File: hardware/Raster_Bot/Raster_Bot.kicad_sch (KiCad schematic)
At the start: 68 parts, among them J1 JST_PH, J2 USB_C_Receptacle_USB2.0_16P, J3 Conn_Motor_N20_Encoder, J4 Conn_EYESPI, J5 JUMPER_2PIN, J6 Conn_Motor_N20_Encoder, J8 JUMPER_2PIN, Q1 AO3401A, SW1 SW_SPDT_SH, SW2 SW_RESET, SW3 SW_BOOT, U1 BQ24072RGT, U2 ESP32-S3-WROOM-1, U3 DRV8833PWPR, U4 AP2114H-3.3, U5 TPS61023DRLR

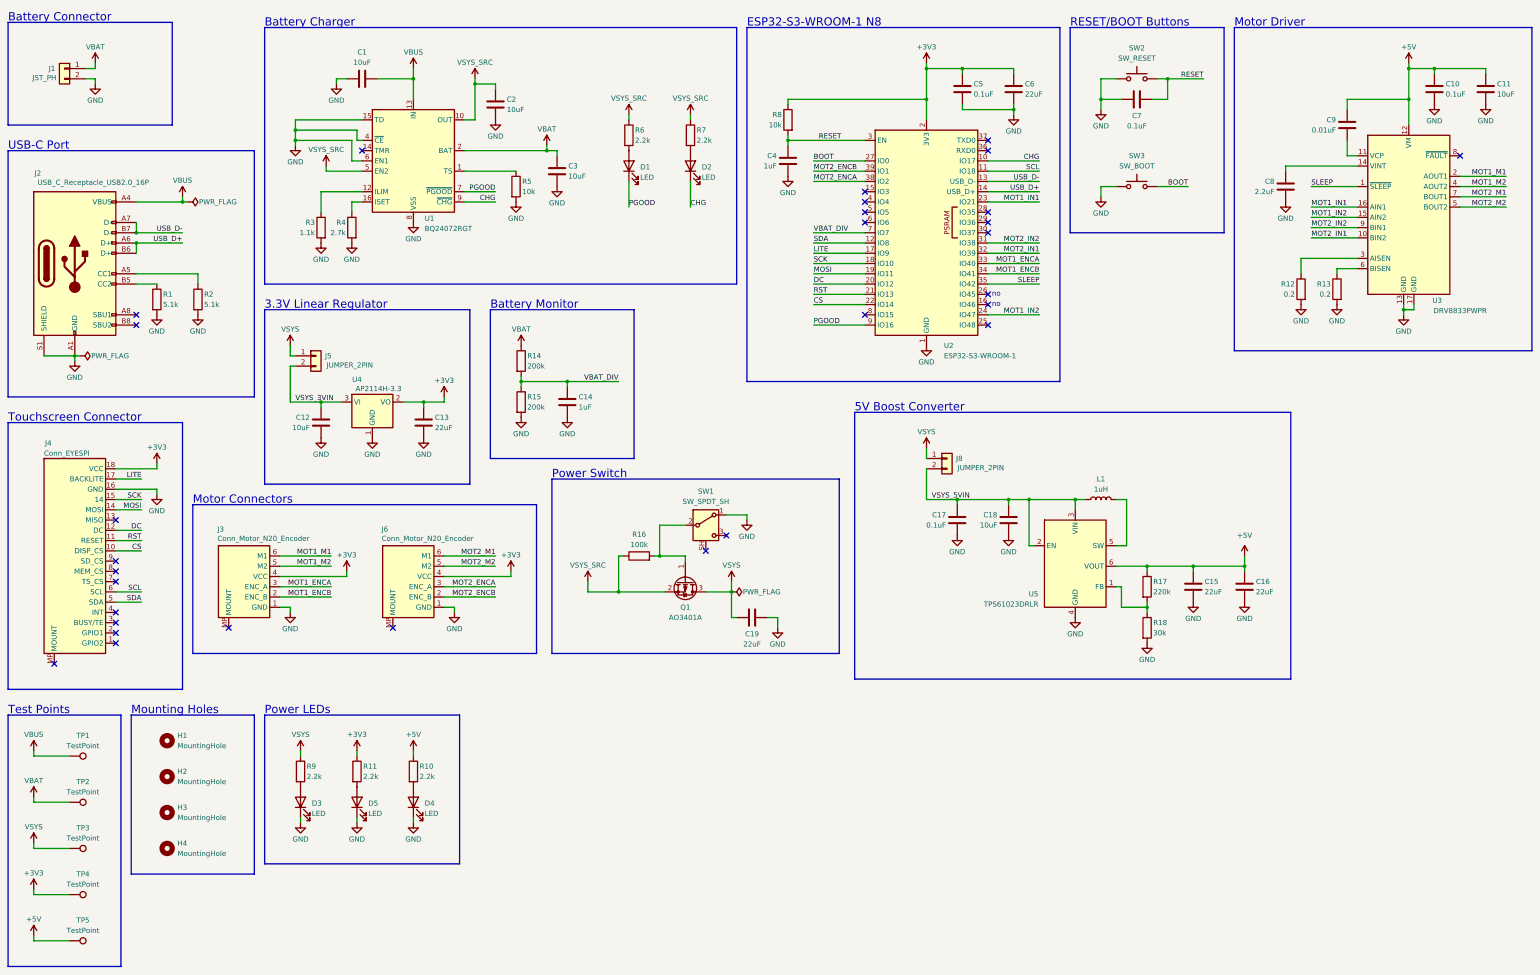
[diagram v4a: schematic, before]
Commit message: [hardware] v0.4 - 4 layer PCB design with ESP32-S3-MINI
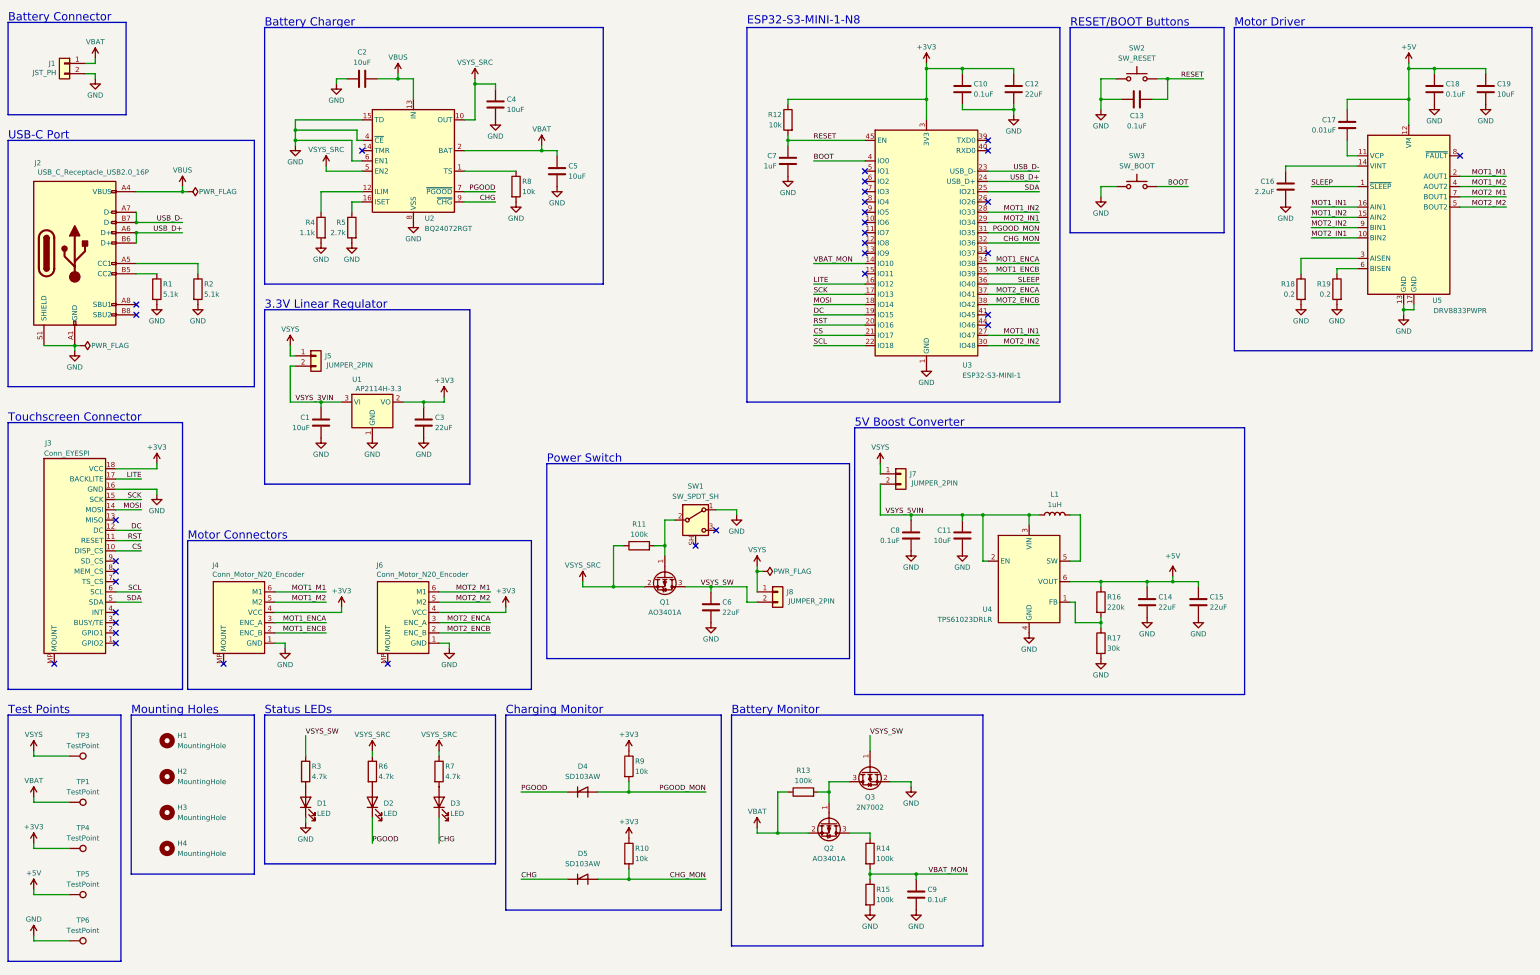
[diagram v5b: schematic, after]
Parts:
- removed C14, C4: 1uF, Capacitor_SMD:C_0603_1608Metric, symbol Device:C
- removed C19: 22uF, Capacitor_SMD:C_0805_2012Metric, symbol Device:C
- removed C5: 0.1uF, Capacitor_SMD:C_0603_1608Metric, symbol Device:C
- removed D4, D5: LED, LED_SMD:LED_0805_2012Metric, symbol Device:LED
- removed R16: 100k, Resistor_SMD:R_0603_1608Metric, symbol Device:R
- removed R8: 10k, Resistor_SMD:R_0603_1608Metric, symbol Device:R
- removed TP2: TestPoint, TestPoint:TestPoint_Pad_1.5x1.5mm, symbol Connector:TestPoint
- removed U2: ESP32-S3-WROOM-1, Raster_Bot:ESP32-S3-WROOM-1, symbol RF_Module:ESP32-S3-WROOM-1
- added C10, C9: 0.1uF, Capacitor_SMD:C_0603_1608Metric, symbol Device:C
- added C12: 22uF, Capacitor_SMD:C_0805_2012Metric, symbol Device:C
- added C7: 1uF, Capacitor_SMD:C_0603_1608Metric, symbol Device:C
- added D4, D5: SD103AW, Diode_SMD:D_SOD-123, symbol Device:D_Shockley
- added J8: JUMPER_2PIN, Connector_PinHeader_2.54mm:PinHeader_1x02_P2.54mm_Vertical, symbol Connector_Generic:Conn_01x02
- added Q2: AO3401A, Package_TO_SOT_SMD:SOT-23, symbol Transistor_FET:AO3401A
- added Q3: 2N7002, Package_TO_SOT_SMD:SOT-23, symbol Transistor_FET:2N7002
- added R12, R9: 10k, Resistor_SMD:R_0603_1608Metric, symbol Device:R
- added R13: 100k, Resistor_SMD:R_0603_1608Metric, symbol Device:R
- added TP6: TestPoint, TestPoint:TestPoint_Pad_1.5x1.5mm, symbol Connector:TestPoint
- added U3: ESP32-S3-MINI-1, Raster_Bot:ESP32-S3-MINI-1, symbol RF_Module:ESP32-S3-MINI-1
- H1, H2, H3, H4: footprint MountingHole:MountingHole_3.2mm_M3 -> MountingHole:MountingHole_2.7mm_M2.5
- R10: value 2.2k -> 10k; LCSC C4190 -> C25804
- R11: value 2.2k -> 100k; LCSC C4190 -> C25803
- R14, R15: value 200k -> 100k; LCSC C25811 -> C25803
- R3: renamed from R9; value 2.2k -> 4.7k; LCSC C4190 -> C23162
- R6, R7: value 2.2k -> 4.7k; LCSC C4190 -> C23162
- renumbered C12 to C1, C18 to C11, C7 to C13, C15 to C14, C16 to C15, C8 to C16, C9 to C17, C10 to C18, C11 to C19, C1 to C2, C13 to C3, C2 to C4, C3 to C5, C17 to C8, D3 to D1, D1 to D2, D2 to D3, J4 to J3, J3 to J4, J8 to J7, R17 to R16, R18 to R17, R12 to R18, R13 to R19, R3 to R4, R4 to R5, R5 to R8, U4 to U1, U1 to U2, U5 to U4, U3 to U5
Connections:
- net +3V3: now also R10.1, C10.1, C12.1, R12.1, R9.1, U3.3 (3V3); no longer C6.1, R11.1
- net +5V: no longer R10.1
- net BOOT: now also U3.4 (IO0)
- net CHG: now also D5.1 (K)
- net CS: now also U3.21 (IO17)
- net DC: now also U3.19 (IO15)
- net GND: now also C10.2, C12.2, C7.2, C9.2, Q3.2 (S), TP6.1, U3.1 (GND), U3.2 (GND), U3.42 (GND), U3.43 (GND), U3.46 (GND), U3.47 (GND), U3.48 (GND), U3.49 (GND), U3.50 (GND), U3.51 (GND), U3.52 (GND), U3.53 (GND), U3.54 (GND), U3.55 (GND), U3.56 (GND), U3.57 (GND), U3.58 (GND), U3.59 (GND), U3.60 (GND), U3.61 (GND), U3.62 (GND), U3.63 (GND), U3.64 (GND), U3.65 (GND)
- net LITE: now also U3.16 (IO12)
- net MOSI: now also U3.18 (IO14)
- net MOT1_ENCA: now also U3.34 (IO38)
- net MOT1_ENCB: now also U3.35 (IO39)
- net MOT1_IN1: now also U3.27 (IO47)
- net MOT1_IN2: now also U3.28 (IO33)
- net MOT2_ENCA: now also U3.37 (IO41)
- net MOT2_ENCB: now also U3.38 (IO42)
- net MOT2_IN1: now also U3.29 (IO34)
- net MOT2_IN2: now also U3.30 (IO48)
- net PGOOD: now also D4.1 (K)
- net RESET: now also C7.1, R12.2, U3.45 (EN)
- net RST: now also U3.20 (IO16)
- net SCK: now also U3.17 (IO13)
- net SCL: now also U3.22 (IO18)
- net SDA: now also U3.25 (IO21)
- net SLEEP: now also U3.36 (IO40)
- net USB_D+: now also U3.24 (USB_D+)
- net USB_D-: now also U3.23 (USB_D-)
- net VBAT: now also TP1.1, Q2.2 (S), R13.1; no longer R14.1
- net VBUS: no longer TP1.1
- net VSYS: now also J8.1 (Pin_1); no longer Q1.3 (D), R3.1
- net VSYS_SRC: now also R11.1
- net at R11.2: now also Q1.1 (G), SW1.2 (B)
- net CHG_MON: now reaches R10.2
- net CHG_MON: now also D5.2 (A), U3.32 (IO36)
- net VBAT_DIV renamed VBAT_MON
- net VBAT_MON: now also C9.1, U3.14 (IO10)
- new net: Q2.3 (D), R14.1
- new net: Q2.1 (G), Q3.3 (D), R13.2
- new net PGOOD_MON: D4.2 (A), R9.2, U3.31 (IO35)
- new net VSYS_SW: C6.1, J8.2 (Pin_2), Q1.3 (D), Q3.1 (G), R3.1
- no-connect marks 30 -> 33
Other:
- note added: "Charging Monitor"
- note added: "ESP32-S3-MINI-1-N8"
- note added: "Status LEDs"
- note removed: "ESP32-S3-WROOM-1 N8"
- note removed: "Power LEDs"
- note removed: "no"
- moved on the sheet: C11, C14, C15, C8, D1, D2, D3, J1, J2, J4, J6, J7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

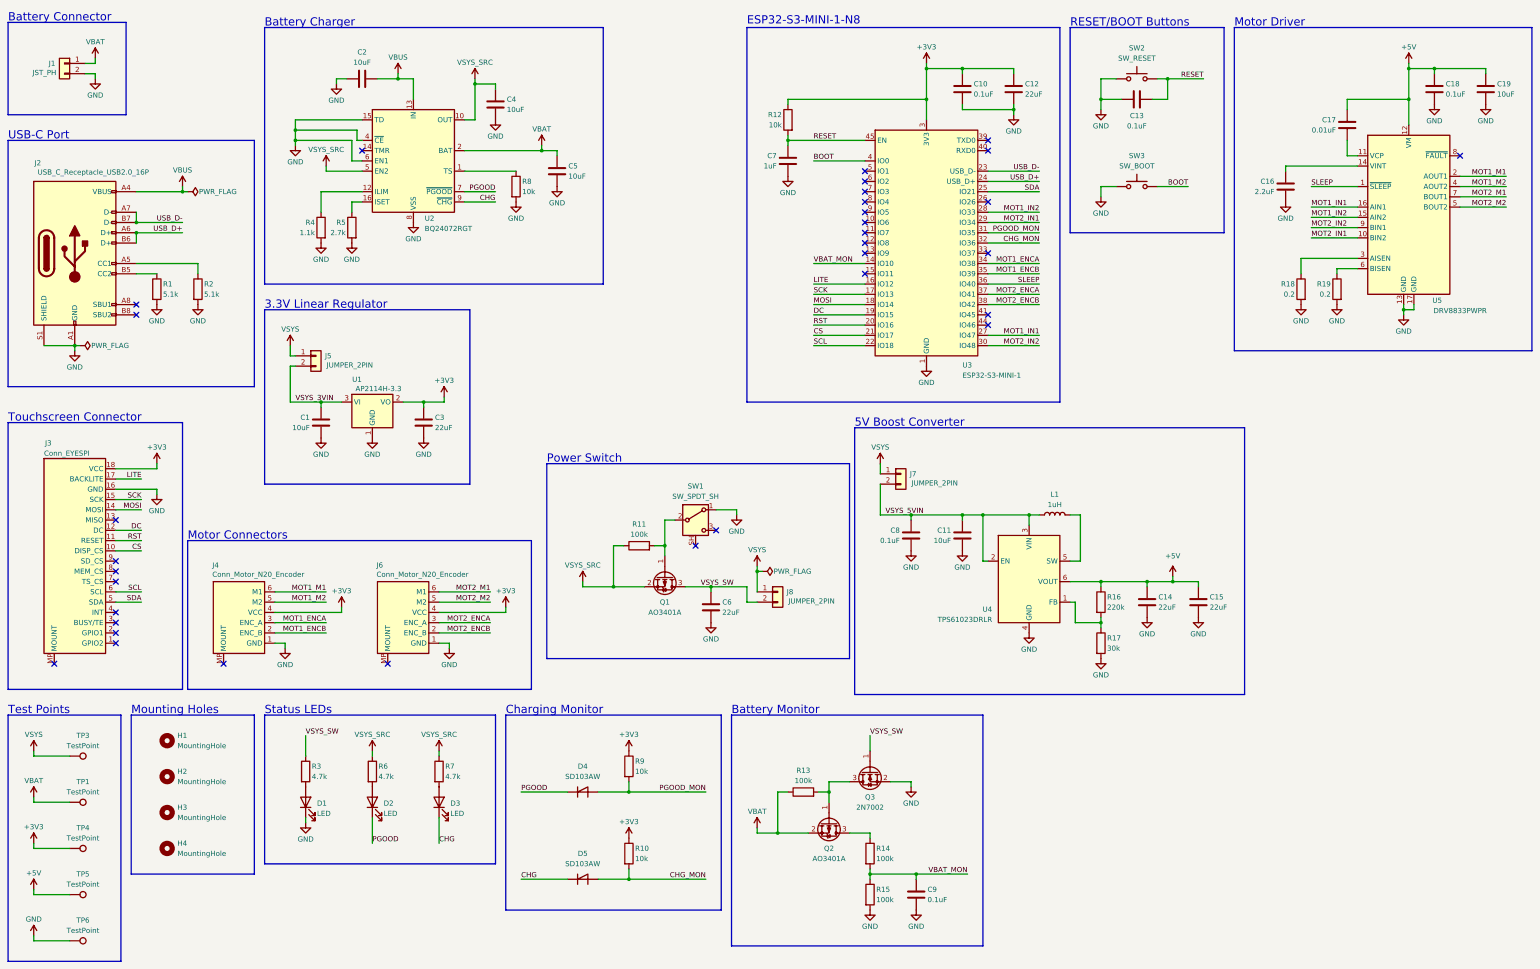
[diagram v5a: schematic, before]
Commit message: [hardware] v0.5 - Add motor driver bulk capacitor; Remove test pads and jumpers
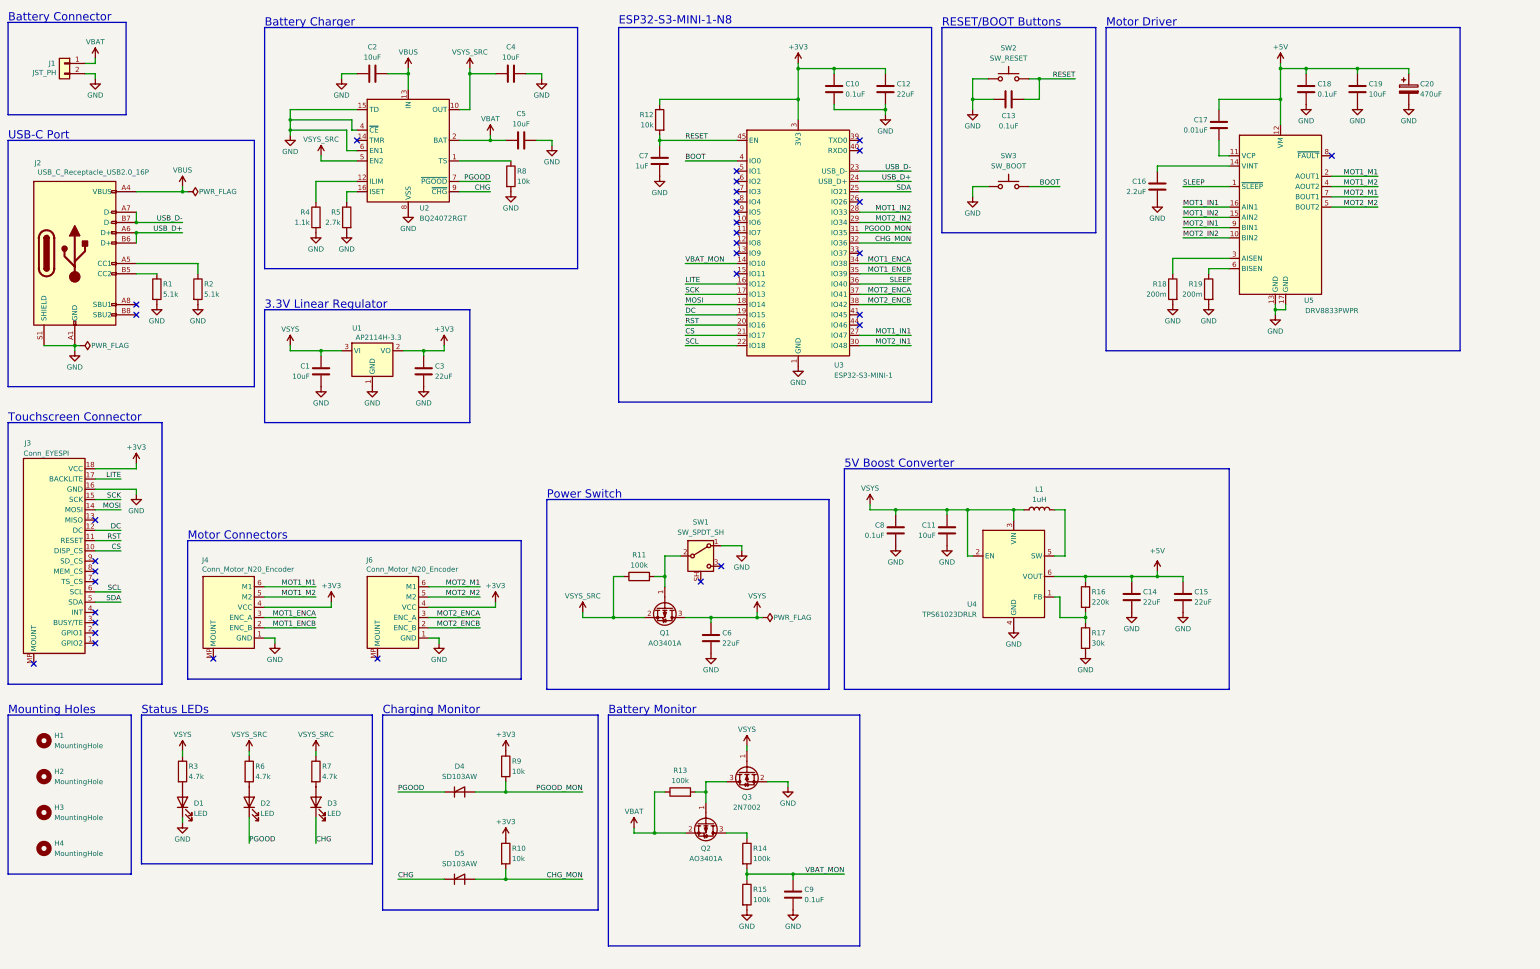
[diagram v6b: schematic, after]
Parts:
- removed J5, J7, J8: JUMPER_2PIN, Connector_PinHeader_2.54mm:PinHeader_1x02_P2.54mm_Vertical, symbol Connector_Generic:Conn_01x02
- removed TP1, TP3, TP4, TP5, TP6: TestPoint, TestPoint:TestPoint_Pad_1.5x1.5mm, symbol Connector:TestPoint
- added C20: 470uF, Capacitor_SMD:CP_Elec_6.3x7.7, symbol Device:C_Polarized
- R18, R19: value 0.2 -> 200m; footprint Resistor_SMD:R_1206_3216Metric -> Resistor_SMD:R_0603_1608Metric; LCSC C7467885 -> (none)
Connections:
- net VSYS_3VIN is gone; now on net VSYS: C1.1, U1.3 (VI)
- net VSYS_5VIN is gone; now on net VSYS: C11.1, C8.1, L1.1, U4.2 (EN), U4.3 (VIN)
- net VSYS_SW is gone; now on net VSYS: C6.1, Q1.3 (D), Q3.1 (G), R3.1
- net +5V: now also C20.1
- net GND: now also C20.2
- net MOT2_IN1: now also U3.30 (IO48), U5.9 (BIN1); no longer U3.29 (IO34), U5.10 (BIN2)
- net MOT2_IN2: now also U3.29 (IO34), U5.10 (BIN2); no longer U3.30 (IO48), U5.9 (BIN1)
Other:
- note removed: "Test Points"
- moved on the sheet: C1, C10, C11, C12, C13, C14, C15, C16, C17, C18, C19, C2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

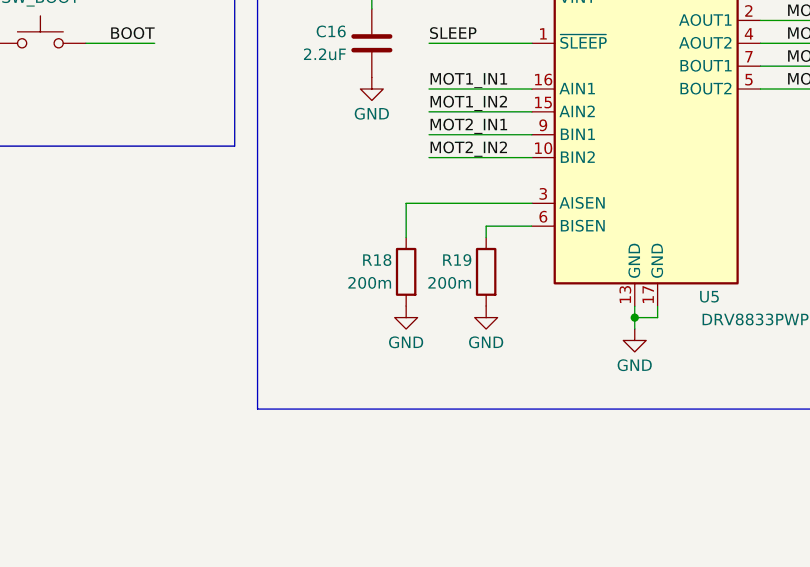
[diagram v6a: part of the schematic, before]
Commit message: [hardware] Chage ISEN resistor values, part, and placement
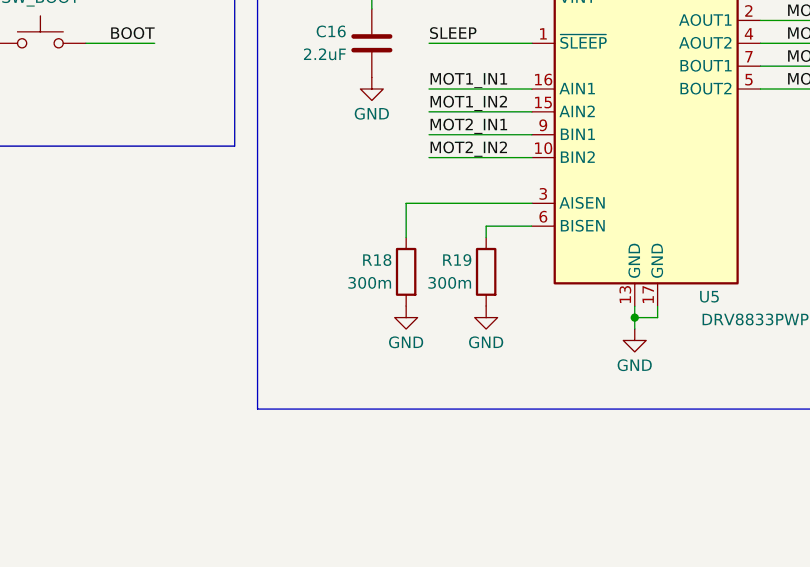
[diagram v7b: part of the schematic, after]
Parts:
- R18, R19: value 200m -> 300m; footprint Resistor_SMD:R_0603_1608Metric -> Resistor_SMD:R_1206_3216Metric; LCSC (none) -> C22464904
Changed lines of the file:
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@@
 			)
 		)
-		(property "Value" "200m"
+		(property "Value" "300m"
 			(at 321.056 101.6 0)
 			(effects
@@
 			)
 		)
-		(property "Footprint" "Resistor_SMD:R_0603_1608Metric"
+		(property "Footprint" "Resistor_SMD:R_1206_3216Metric"
 			(at 324.358 100.33 90)
 			(effects
@@
 			)
 		)
-		(property "LCSC" ""
+		(property "LCSC" "C22464904"
 			(at 322.58 100.33 0)
 			(effects
@@
 			)
 		)
-		(property "Value" "200m"
+		(property "Value" "300m"
 			(at 312.166 101.6 0)
 			(effects
@@
 			)
 		)
-		(property "Footprint" "Resistor_SMD:R_0603_1608Metric"
+		(property "Footprint" "Resistor_SMD:R_1206_3216Metric"
 			(at 315.468 100.33 90)
 			(effects
@@
 			)
 		)
-		(property "LCSC" ""
+		(property "LCSC" "C22464904"
 			(at 313.69 100.33 0)
 			(effects
